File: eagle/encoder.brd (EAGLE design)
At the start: 100 x 80 mm, 31 parts, among them IC1 LM339D, J1 SPI, U1 MCP42XXX, U2 ATMEGA328P

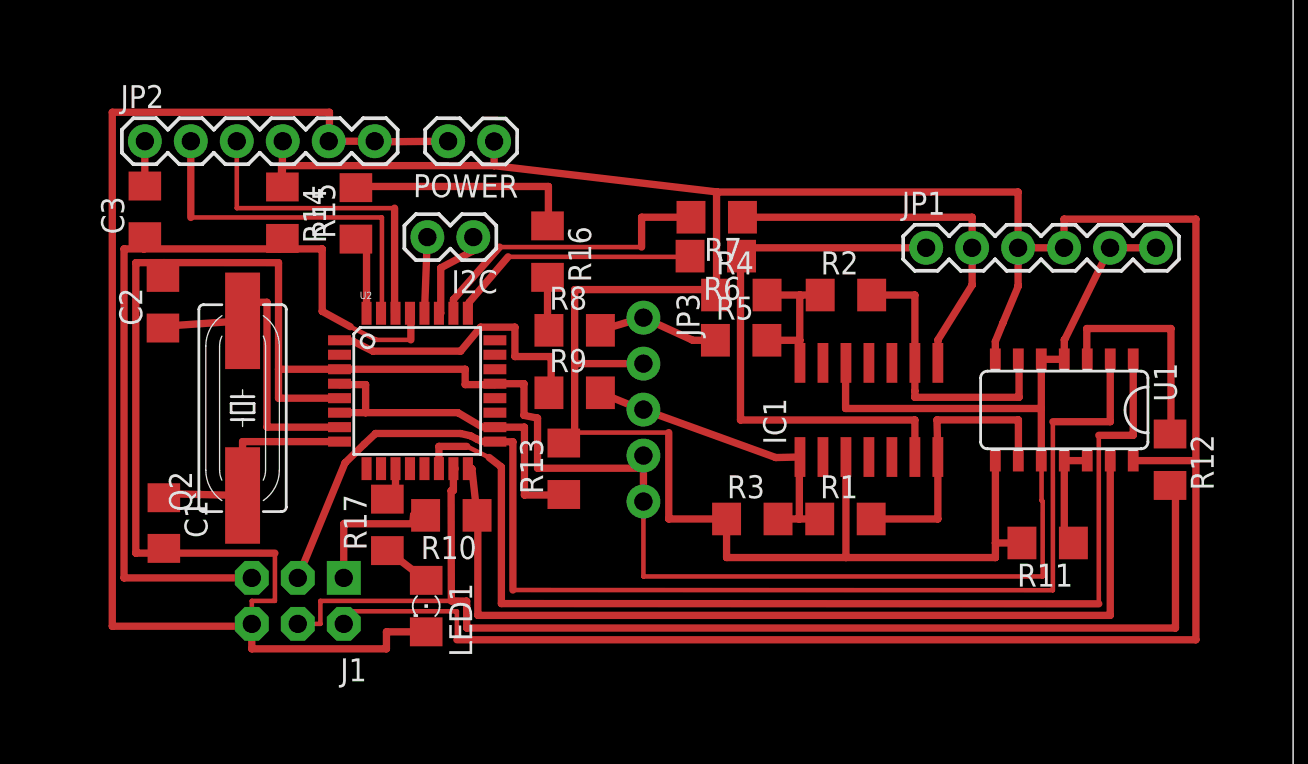
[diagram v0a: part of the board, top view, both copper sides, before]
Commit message: Made corners 45 degrees as opposed to 90.
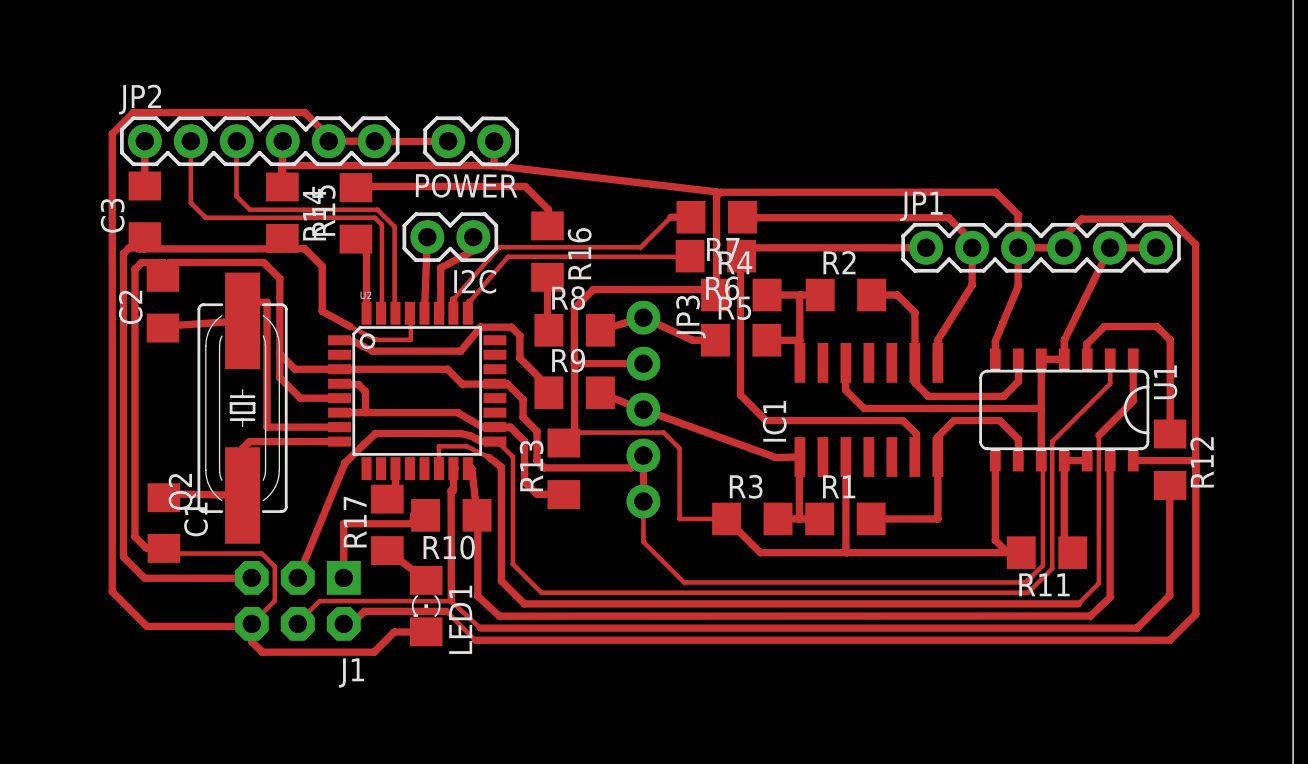
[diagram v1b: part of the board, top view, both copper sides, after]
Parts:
- JP1: value (none) -> Sensor
- JP3: value (none) -> Enc Out
- moved R11 0.54 mm to (86.4, 41.3)
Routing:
- net GND: track 207.6 -> 201.3 mm
- net +5V: track 212.2 -> 207.0 mm
- net SCK: track 70.9 -> 67.1 mm
- net MOSI: track 67.0 -> 64.0 mm
- net SS: track 61.0 -> 58.5 mm
- net B-REF: track 15.9 -> 14.3 mm
- net N$7: track 16.2 -> 15.0 mm
- net RESET: track 47.8 -> 46.6 mm
- net A-REF: track 15.9 -> 14.7 mm
- net MISO: track 51.9 -> 50.7 mm
- net N$3: track 31.4 -> 30.3 mm
- net N$9: track 18.7 -> 17.6 mm
- net RX-I: track 18.3 -> 17.3 mm
- net A-ANALOG-IN: track 16.8 -> 15.9 mm
- net N$8: track 12.3 -> 11.4 mm
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
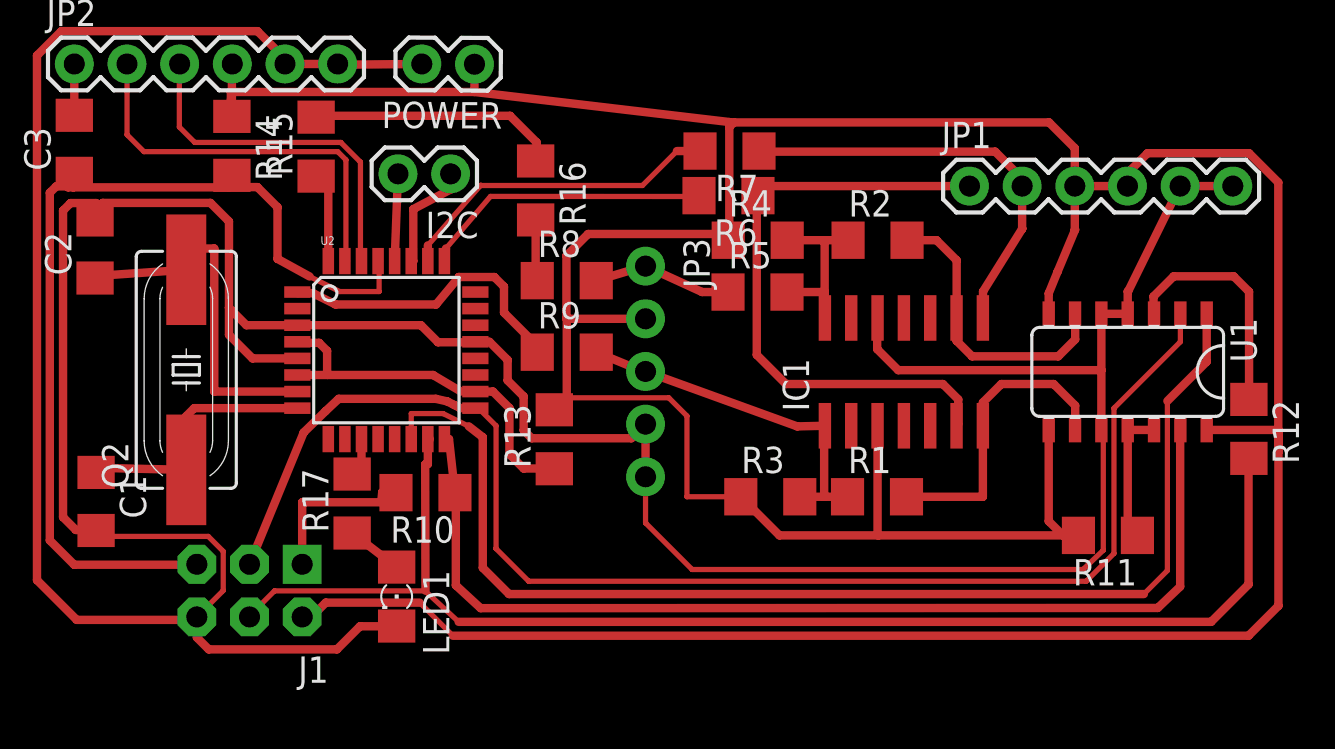
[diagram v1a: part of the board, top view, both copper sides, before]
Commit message: Hacked pads for lm339 to be larger
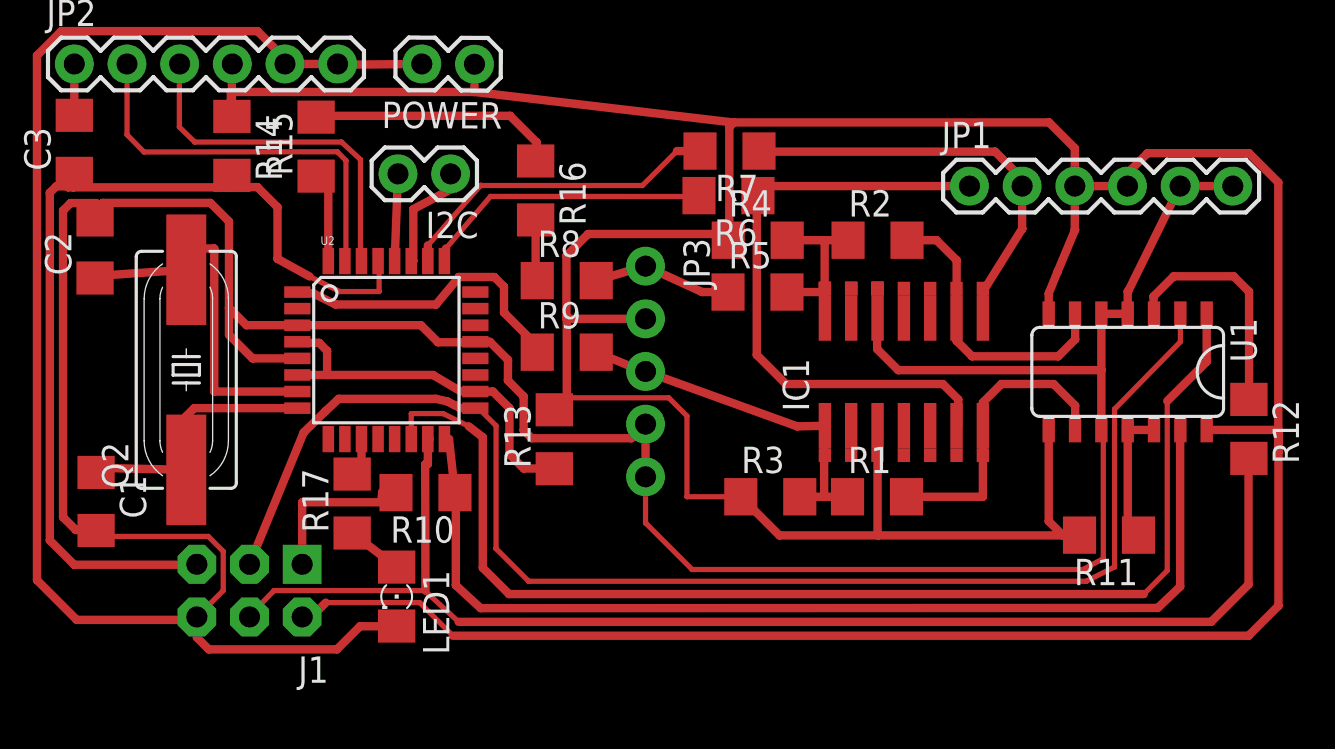
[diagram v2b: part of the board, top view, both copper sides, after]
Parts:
- moved R11 0.05 mm to (86.5, 41.3)

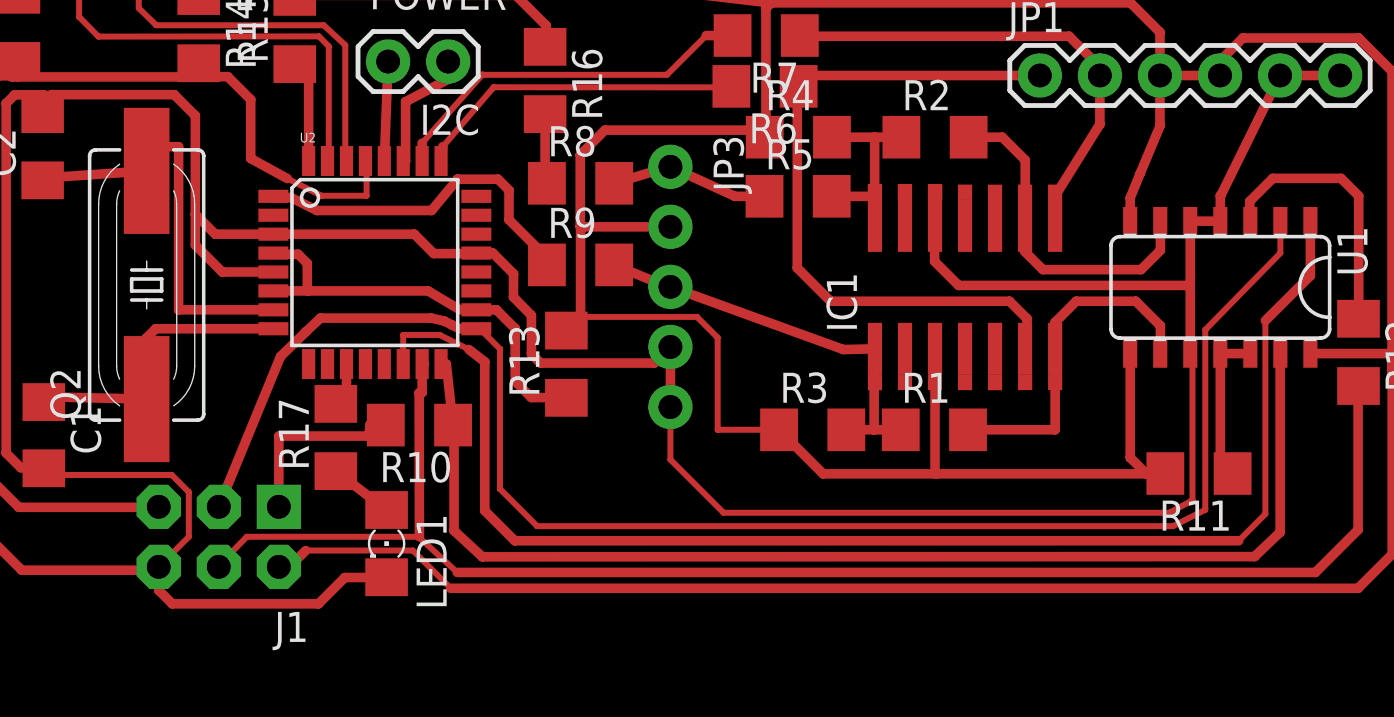
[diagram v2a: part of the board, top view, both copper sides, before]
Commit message: Fixed some additional corners to be 45 degrees instead of 90.
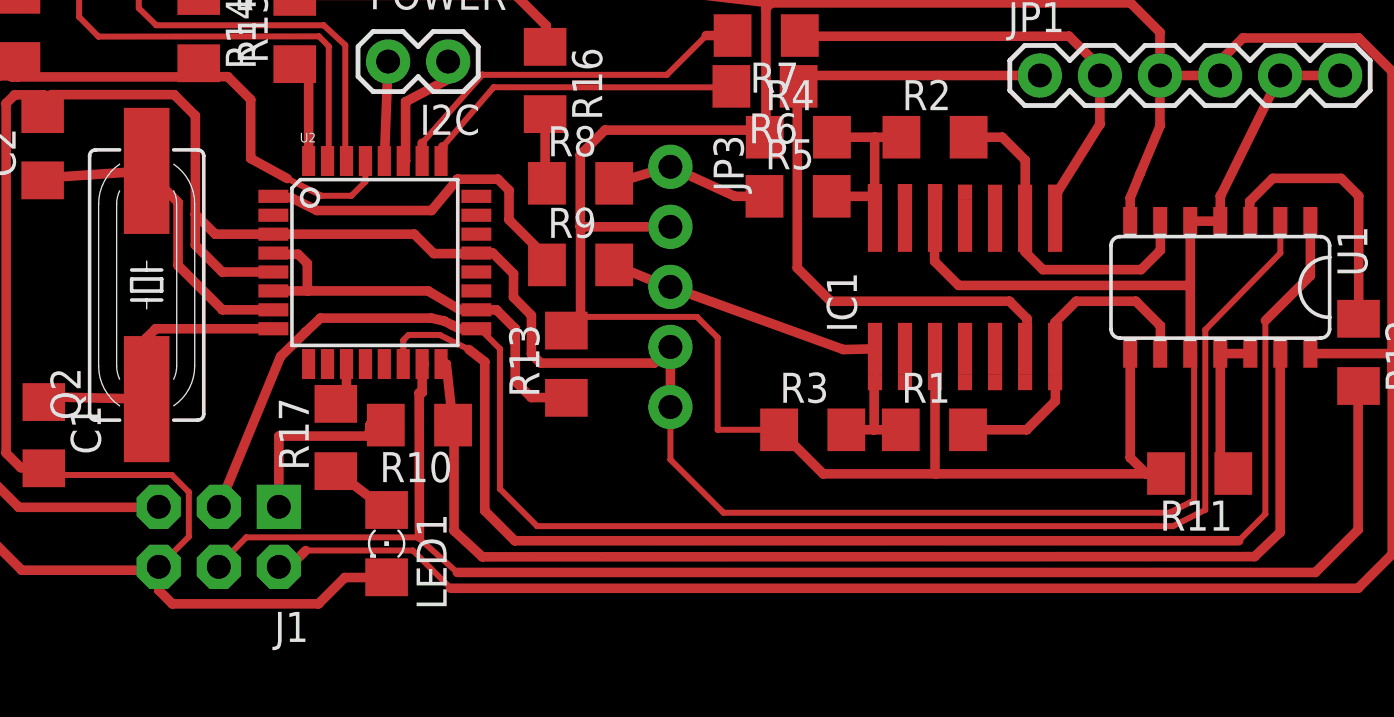
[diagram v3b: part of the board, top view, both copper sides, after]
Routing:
- net N$11: track 17.8 -> 14.9 mm
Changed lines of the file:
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@@
 <element name="R10" library="resistor" package="R1206" value="0" x="53.48570625" y="43.375321875" rot="R180"/>
 <element name="J1" library="SparkFun-Connectors" package="2X3-NS" value="SPI" x="45" y="38.65" rot="R180"/>
-<element name="R11" library="resistor" package="R1206" value="0" x="86.45285" y="41.326584375" rot="R180"/>
+<element name="R11" library="resistor" package="R1206" value="0" x="86.481803125" y="41.326584375" rot="R180"/>
 <element name="R12" library="resistor" package="R1206" value="0" x="93.2" y="46.45" rot="R270"/>
 <element name="R13" library="resistor" package="R1206" value="0" x="59.7" y="45.95" rot="R90"/>
@@
 <wire x1="64.1" y1="41.91383125" x2="66.34571875" y2="39.6681125" width="0.254" layer="1"/>
 <wire x1="66.34571875" y1="39.6681125" x2="85.1985" y2="39.6681125" width="0.254" layer="1"/>
-<wire x1="85.1985" y1="39.6681125" x2="86.177315625" y2="40.192965625" width="0.254" layer="1"/>
-<wire x1="86.177315625" y1="40.192965625" x2="86.177315625" y2="46.35919375" width="0.254" layer="1"/>
-<wire x1="86.177315625" y1="46.35919375" x2="86.085" y2="46.4" width="0.254" layer="1"/>
+<wire x1="85.1985" y1="39.6681125" x2="86.246984375" y2="40.192965625" width="0.254" layer="1"/>
+<wire x1="86.246984375" y1="40.192965625" x2="86.246984375" y2="46.35919375" width="0.254" layer="1"/>
+<wire x1="86.246984375" y1="46.35919375" x2="86.085" y2="46.4" width="0.254" layer="1"/>
 <wire x1="75.271946875" y1="51.8" x2="75.271946875" y2="50.29805625" width="0.4064" layer="1"/>
 <wire x1="75.271946875" y1="50.29805625" x2="76.2882875" y2="49.281715625" width="0.4064" layer="1"/>
@@
 <contactref element="POWER" pad="1"/>
 <wire x1="55.85" y1="64.037015625" x2="55.85" y2="62.7" width="0.4064" layer="1"/>
-<wire x1="85.03085" y1="41.326584375" x2="84.229634375" y2="41.3136875" width="0.4064" layer="1"/>
+<wire x1="85.059803125" y1="41.326584375" x2="84.229634375" y2="41.3136875" width="0.4064" layer="1"/>
 <wire x1="84.229634375" y1="41.3136875" x2="75.32760625" y2="41.3136875" width="0.4064" layer="1"/>
 <wire x1="75.32760625" y1="41.3136875" x2="70.557490625" y2="41.3136875" width="0.4064" layer="1"/>
@@
 <contactref element="R1" pad="2"/>
 <contactref element="IC1" pad="7"/>
-<wire x1="76.685440625" y1="43.17635625" x2="80.37" y2="43.17635625" width="0.4064" layer="1"/>
-<wire x1="80.37" y1="43.17635625" x2="80.37" y2="46.6" width="0.4064" layer="1"/>
 <wire x1="84.815" y1="46.4" x2="84.820821875" y2="46.4" width="0.4064" layer="1"/>
-<wire x1="80.37" y1="46.6" x2="80.37" y2="47.72335625" width="0.4064" layer="1"/>
+<wire x1="80.37" y1="46.6" x2="80.37" y2="47.11638125" width="0.4064" layer="1"/>
+<wire x1="80.37" y1="47.11638125" x2="80.37" y2="47.72335625" width="0.4064" layer="1"/>
 <wire x1="80.37" y1="47.72335625" x2="81.260384375" y2="48.613740625" width="0.4064" layer="1"/>
 <wire x1="81.260384375" y1="48.613740625" x2="83.783409375" y2="48.613740625" width="0.4064" layer="1"/>
@@
 <wire x1="84.82248125" y1="47.57466875" x2="84.82248125" y2="46.40748125" width="0.4064" layer="1"/>
 <wire x1="84.82248125" y1="46.40748125" x2="84.815" y2="46.4" width="0.4064" layer="1"/>
+<wire x1="76.685440625" y1="43.17635625" x2="79.165084375" y2="43.17635625" width="0.4064" layer="1"/>
+<wire x1="79.165084375" y1="43.17635625" x2="80.37936875" y2="44.390640625" width="0.4064" layer="1"/>
+<wire x1="80.37936875" y1="44.390640625" x2="80.37936875" y2="47.1070125" width="0.4064" layer="1"/>
+<wire x1="80.37936875" y1="47.1070125" x2="80.37" y2="47.11638125" width="0.4064" layer="1"/>
 </signal>
 <signal name="N$1">
@@
 <wire x1="93.2" y1="45.028" x2="93.5" y2="45.028" width="0.4064" layer="1"/>
 <wire x1="45" y1="37.38" x2="45" y2="37.43271875" width="0.254" layer="1"/>
-<wire x1="45" y1="37.43271875" x2="46.18266875" y2="38.652696875" width="0.254" layer="1"/>
-<wire x1="46.18266875" y1="38.652696875" x2="53.445484375" y2="38.652696875" width="0.254" layer="1"/>
-<wire x1="53.445484375" y1="38.652696875" x2="55.085525" y2="37.143778125" width="0.254" layer="1"/>
+<wire x1="45" y1="37.43271875" x2="46.157646875" y2="38.627675" width="0.254" layer="1"/>
+<wire x1="46.157646875" y1="38.627675" x2="53.4204625" y2="38.627675" width="0.254" layer="1"/>
+<wire x1="53.4204625" y1="38.627675" x2="55.085525" y2="37.143778125" width="0.254" layer="1"/>
 <wire x1="55.085525" y1="37.143778125" x2="91.37966875" y2="37.143778125" width="0.4064" layer="1"/>
 <wire x1="91.37966875" y1="37.143778125" x2="93.182765625" y2="38.946875" width="0.4064" layer="1"/>
 <wire x1="93.182765625" y1="38.946875" x2="93.182765625" y2="45.010765625" width="0.4064" layer="1"/>
 <wire x1="93.182765625" y1="45.010765625" x2="93.2" y2="45.028" width="0.254" layer="1"/>
-<wire x1="53.445484375" y1="38.652696875" x2="53.48570625" y2="38.64935625" width="0" layer="19" extent="1-1"/>
+<wire x1="53.4204625" y1="38.627675" x2="53.48570625" y2="38.64935625" width="0" layer="19" extent="1-1"/>
 </signal>
 <signal name="MISO">
@@
 <signal name="RESET">
 <contactref element="U2" pad="29"/>
-<wire x1="51.2" y1="54.5426" x2="51.25" y2="54.5426" width="0.4064" layer="1"/>
-<wire x1="51.25" y1="54.5426" x2="51.25" y2="53.073384375" width="0.254" layer="1"/>
-<wire x1="51.25" y1="53.073384375" x2="49.35" y2="53.073384375" width="0.254" layer="1"/>
+<wire x1="51.2" y1="54.5426" x2="51.25" y2="54.5426" width="0.254" layer="1"/>
 <wire x1="49.35" y1="53.073384375" x2="47.9" y2="53.8" width="0.254" layer="1"/>
 <wire x1="47.9" y1="53.8" x2="46.35" y2="54.65" width="0.4064" layer="1"/>
@@
 <wire x1="45.380884375" y1="58.111209375" x2="44.011209375" y2="58.111209375" width="0.4064" layer="1"/>
 <wire x1="44.011209375" y1="58.111209375" x2="44" y2="58.1" width="0.4064" layer="1"/>
+<wire x1="49.35" y1="53.073384375" x2="50.606190625" y2="53.073384375" width="0.254" layer="1"/>
+<wire x1="50.606190625" y1="53.073384375" x2="51.197775" y2="53.66496875" width="0.254" layer="1"/>
+<wire x1="51.197775" y1="53.66496875" x2="51.197775" y2="54.540375" width="0.254" layer="1"/>
+<wire x1="51.197775" y1="54.540375" x2="51.2" y2="54.5426" width="0.254" layer="1"/>
 </signal>
 <signal name="SS">
 <contactref element="U1" pad="1"/>
 <contactref element="U2" pad="14"/>
-<wire x1="52.8" y1="45.9574" x2="52.8" y2="47.18830625" width="0.254" layer="1"/>
-<wire x1="52.8" y1="47.18830625" x2="54.33961875" y2="47.18830625" width="0.254" layer="1"/>
 <wire x1="54.33961875" y1="47.18830625" x2="55.574675" y2="46.574675" width="0.254" layer="1"/>
 <wire x1="55.574675" y1="46.574675" x2="56.25" y2="46.05" width="0.4064" layer="1"/>
@@
 <wire x1="91.165" y1="52" x2="91.165" y2="49.691425" width="0.4064" layer="1"/>
 <wire x1="91.165" y1="49.691425" x2="89.2617375" y2="47.79438125" width="0.4064" layer="1"/>
+<wire x1="54.33961875" y1="47.18830625" x2="53.024090625" y2="47.18830625" width="0.254" layer="1"/>
+<wire x1="53.024090625" y1="47.18830625" x2="52.804178125" y2="46.96839375" width="0.254" layer="1"/>
+<wire x1="52.804178125" y1="46.96839375" x2="52.804178125" y2="45.961578125" width="0.254" layer="1"/>
+<wire x1="52.804178125" y1="45.961578125" x2="52.8" y2="45.9574" width="0.254" layer="1"/>
 </signal>
 <signal name="N$2">
@@
 <contactref element="U1" pad="12"/>
 <contactref element="R11" pad="1"/>
-<wire x1="87.87485" y1="41.326584375" x2="87.355" y2="41.85" width="0.4064" layer="1"/>
+<wire x1="87.903803125" y1="41.326584375" x2="87.355" y2="41.85" width="0.4064" layer="1"/>
 <wire x1="87.355" y1="41.85" x2="87.355" y2="46.4" width="0.4064" layer="1"/>
 <wire x1="87.355" y1="46.4" x2="88.625" y2="46.4" width="0.4064" layer="1"/>
@@
 <contactref element="Q2" pad="2"/>
 <contactref element="C2" pad="1"/>
-<wire x1="47.3074" y1="48.25" x2="43.3" y2="48.25" width="0.4064" layer="1"/>
-<wire x1="43.3" y1="48.25" x2="43.3" y2="55.15" width="0.4064" layer="1"/>
-<wire x1="43.3" y1="55.15" x2="41.95" y2="55.15" width="0.4064" layer="1"/>
 <wire x1="41.95" y1="55.15" x2="41.95" y2="54.126" width="0.4064" layer="1"/>
 <wire x1="41.95" y1="54.126" x2="37.6" y2="53.826" width="0.4064" layer="1"/>
 <wire x1="37.6" y1="53.826" x2="37.55" y2="53.725965625" width="0.4064" layer="1"/>
+<wire x1="47.3074" y1="48.25" x2="45.156028125" y2="48.25" width="0.4064" layer="1"/>
+<wire x1="45.156028125" y1="48.25" x2="43.275775" y2="50.130253125" width="0.4064" layer="1"/>
+<wire x1="43.275775" y1="50.130253125" x2="43.275775" y2="52.800225" width="0.4064" layer="1"/>
+<wire x1="43.275775" y1="52.800225" x2="41.95" y2="54.126" width="0.4064" layer="1"/>
 </signal>
 <signal name="DTR">
